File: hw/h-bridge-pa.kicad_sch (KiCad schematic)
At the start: 15 parts, among them Q2301 EPC2037, Q2302 EPC2037, Q2303 IGB110S101XTMA1, Q2304 IGB110S101XTMA1, Q502 IGB110S101XTMA1, Q503 IGB110S101XTMA1, U2301 LMG1210RVRR, U503 LMG1210RVRR

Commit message: Now using H bridge for differential QSE based I/Q tx
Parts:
- T2301: renamed from T502; symbol Device:L_Ferrite_Coupled_Small -> Device:L_Iron_Coupled
- renumbered C2302 to C2301, C2304 to C2302, C2305 to C2304, C2301 to C2305, Q502 to Q2303, Q503 to Q2304, Q2303 to Q2305, Q2304 to Q2306, U503 to U2301, U2301 to U2302
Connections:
- net at Q2303.10 (S), Q2303.11 (S), Q2303.12 (S)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: now also C2305.2, U2301.13 (HS), U2301.14 (HS), U2301.16 (HS), U2301.21 (HS_DAP), U2301.9 (HS)
- net at Q2305.10 (S), Q2305.11 (S), Q2305.12 (S)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: now also C2306.2, U2302.13 (HS), U2302.14 (HS), U2302.16 (HS), U2302.21 (HS_DAP), U2302.9 (HS)
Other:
- moved on the sheet: C2301, C2302, C2303, C2304, C2305, C2306, Q2301, Q2302, Q2303, Q2304, Q2305, Q2306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

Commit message: Trying some sims to make sure tx will work as specified
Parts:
- C2301, C2302, C2303, C2304, C2305, C2306: footprint (none) -> Capacitor_SMD:C_0805_2012Metric
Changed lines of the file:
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@@
 			)
 		)
-		(property "Footprint" ""
+		(property "Footprint" "Capacitor_SMD:C_0805_2012Metric"
 			(at 32.0548 130.81 0)
 			(effects
@@
 				)
 				(hide yes)
+			)
+		)
+		(property "cap-type" ""
+			(at 33.02 127 0)
+			(effects
+				(font
+					(size 1.27 1.27)
+				)
+			)
+		)
+		(property "r-power" ""
+			(at 33.02 127 0)
+			(effects
+				(font
+					(size 1.27 1.27)
+				)
 			)
 		)
@@
 			)
 		)
-		(property "Footprint" ""
+		(property "Footprint" "Capacitor_SMD:C_0805_2012Metric"
 			(at 32.0548 46.99 0)
 			(effects
@@
 				)
 				(hide yes)
+			)
+		)
+		(property "cap-type" ""
+			(at 33.02 43.18 0)
+			(effects
+				(font
+					(size 1.27 1.27)
+				)
+			)
+		)
+		(property "r-power" ""
+			(at 33.02 43.18 0)
+			(effects
+				(font
+					(size 1.27 1.27)
+				)
 			)
 		)
@@
 			)
 		)
-		(property "Footprint" ""
+		(property "Footprint" "Capacitor_SMD:C_0805_2012Metric"
 			(at 39.0652 130.81 0)
 			(effects
@@
 			)
 		)
-		(property "Footprint" ""
+		(property "Footprint" "Capacitor_SMD:C_0805_2012Metric"
 			(at 98.0948 50.8 0)
 			(effects
@@
 			)
 		)
-		(property "Footprint" ""
+		(property "Footprint" "Capacitor_SMD:C_0805_2012Metric"
 			(at 98.0948 134.62 0)
 			(effects
@@
 			)
 		)
-		(property "Footprint" ""
+		(property "Footprint" "Capacitor_SMD:C_0805_2012Metric"
 			(at 39.0652 46.99 0)
 			(effects

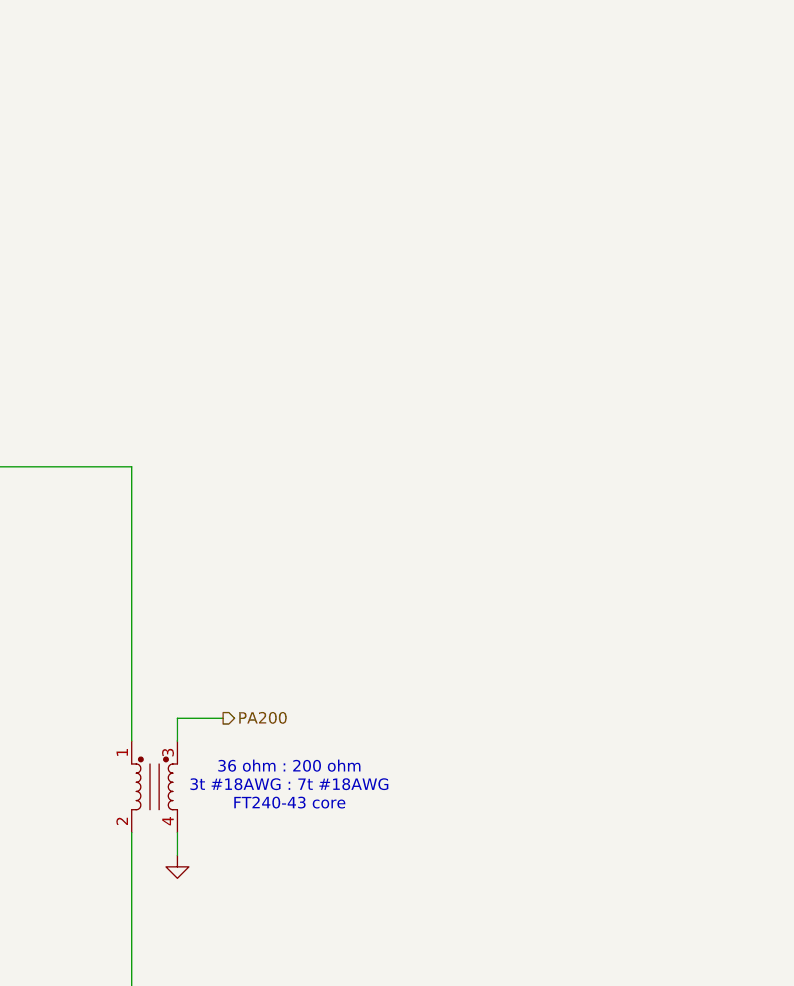
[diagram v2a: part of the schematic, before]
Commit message: Removed PA tanks. LPFs are now 7th order Chebyshev and we are better than -70dBc. Added 0R to power rails for measuring and other testing (did not dare do that for Veer). PCB is now grouped by function to get ready for layout. Still need to verify and set C working voltage levels and choose L and C components for the LPFs. Now using smaller relays at a slight cost premium.
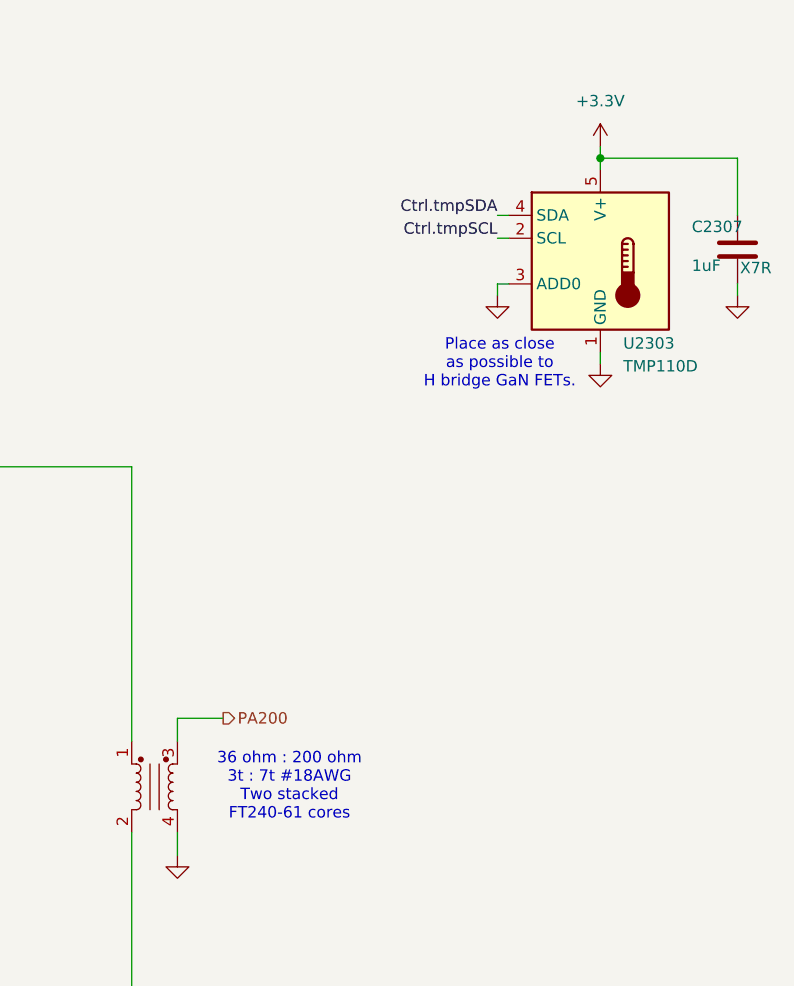
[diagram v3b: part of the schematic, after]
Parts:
- added C2307: 1uF, Capacitor_SMD:C_0805_2012Metric, symbol Device:C
- added U2303: TMP110D, Package_SON:Texas_X2SON-5_0.8x0.8mm_P0.48mm, symbol Sensor_Temperature:TMP110D
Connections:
- net GND: now also C2307.2, U2303.1 (GND), U2303.3 (ADD0)
- new net +3.3V: C2307.1, U2303.5 (V+)
- new net Ctrl.tmpSCL: U2303.2 (SCL)
- new net Ctrl.tmpSDA: U2303.4 (SDA)
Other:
- note added: "36 ohm : 200 ohm 3t : 7t #18AWG Two stacked FT240-61 cores"
- note added: "Place as close as possible to H bridge GaN FETs."
- note removed: "36 ohm : 200 ohm 3t #18AWG : 7t #18AWG FT240-43 core"

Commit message: Starting layout a bit
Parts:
- T2301: footprint Inductor_THT:L_CommonMode_Toroid_Vertical_L38.1mm_W20.3mm_Px15.24mm_Py22.86mm_Bourns_8100 -> Library:2xFT240-stacked
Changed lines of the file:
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@@
 		(dnp no)
 		(property "Reference" "T2301"
-			(at 167.894 102.87 90)
+			(at 173.736 98.552 0)
 			(effects
 				(font
@@
 				)
 				(justify right)
-				(hide yes)
 			)
 		)
@@
 			)
 		)
-		(property "Footprint" "Inductor_THT:L_CommonMode_Toroid_Vertical_L38.1mm_W20.3mm_Px15.24mm_Py22.86mm_Bourns_8100"
+		(property "Footprint" "Library:2xFT240-stacked"
 			(at 173.99 102.87 0)
 			(effects

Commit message: Continuing to route. Net classes can be rather important.
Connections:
- net GND: now also Q2304.10 (S), Q2304.11 (S), Q2304.12 (S), Q2304.3 (S), Q2304.4 (S), Q2304.6 (S), Q2304.7 (S), Q2304.8 (S), Q2304.9 (S), Q2306.10 (S), Q2306.11 (S), Q2306.12 (S), Q2306.3 (S), Q2306.4 (S), Q2306.6 (S), Q2306.7 (S), Q2306.8 (S), Q2306.9 (S)

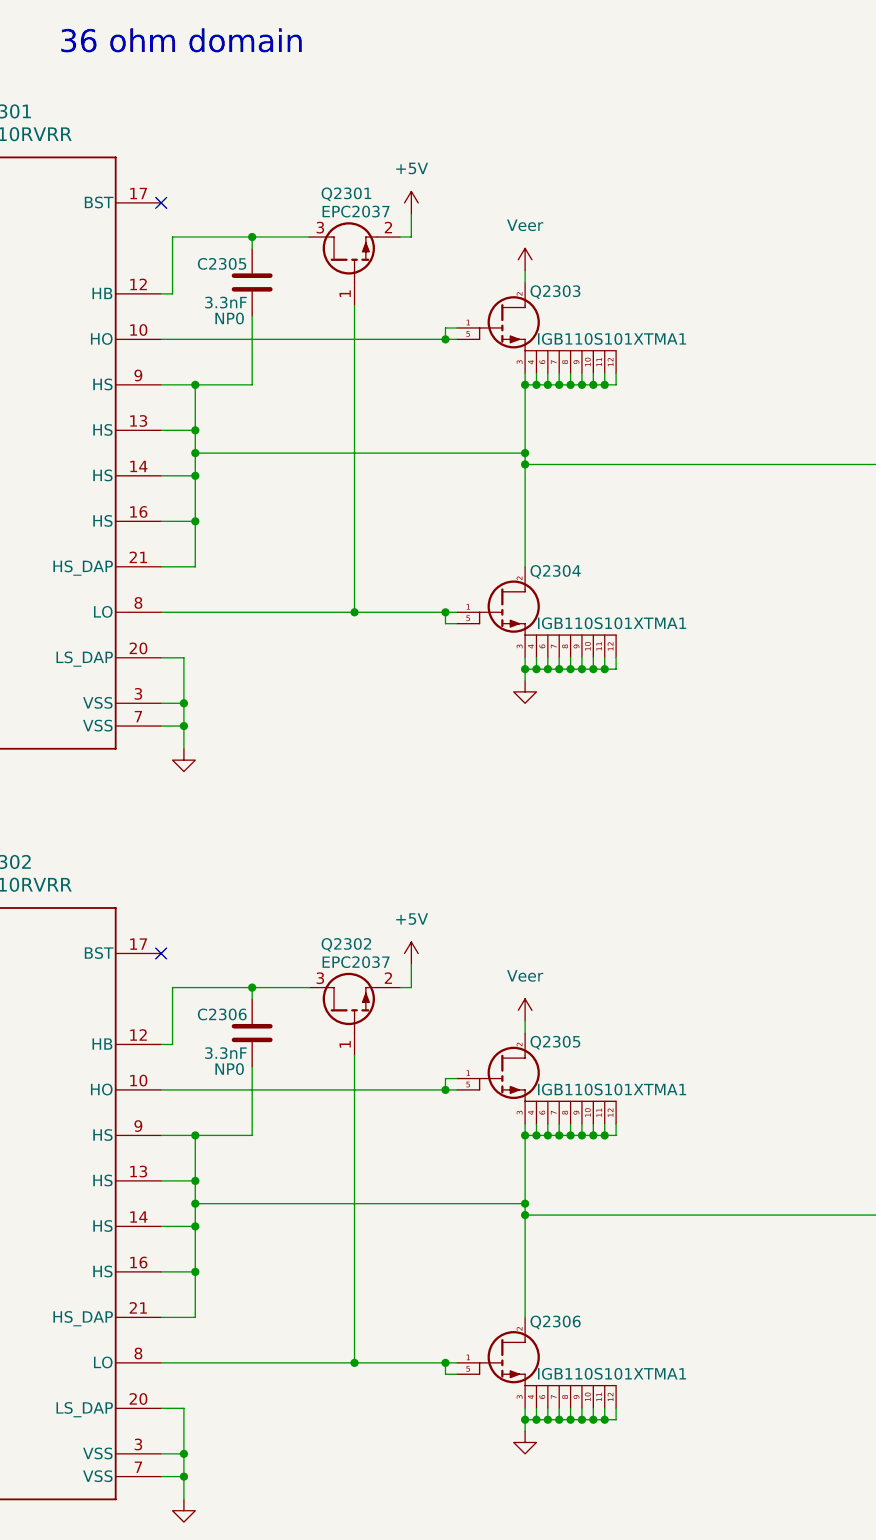
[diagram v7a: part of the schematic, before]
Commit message: I laid down three QSDs but have not done any canyon for 800 ohm yet. Starting to look at Veer buck/boost to round out my understanding.
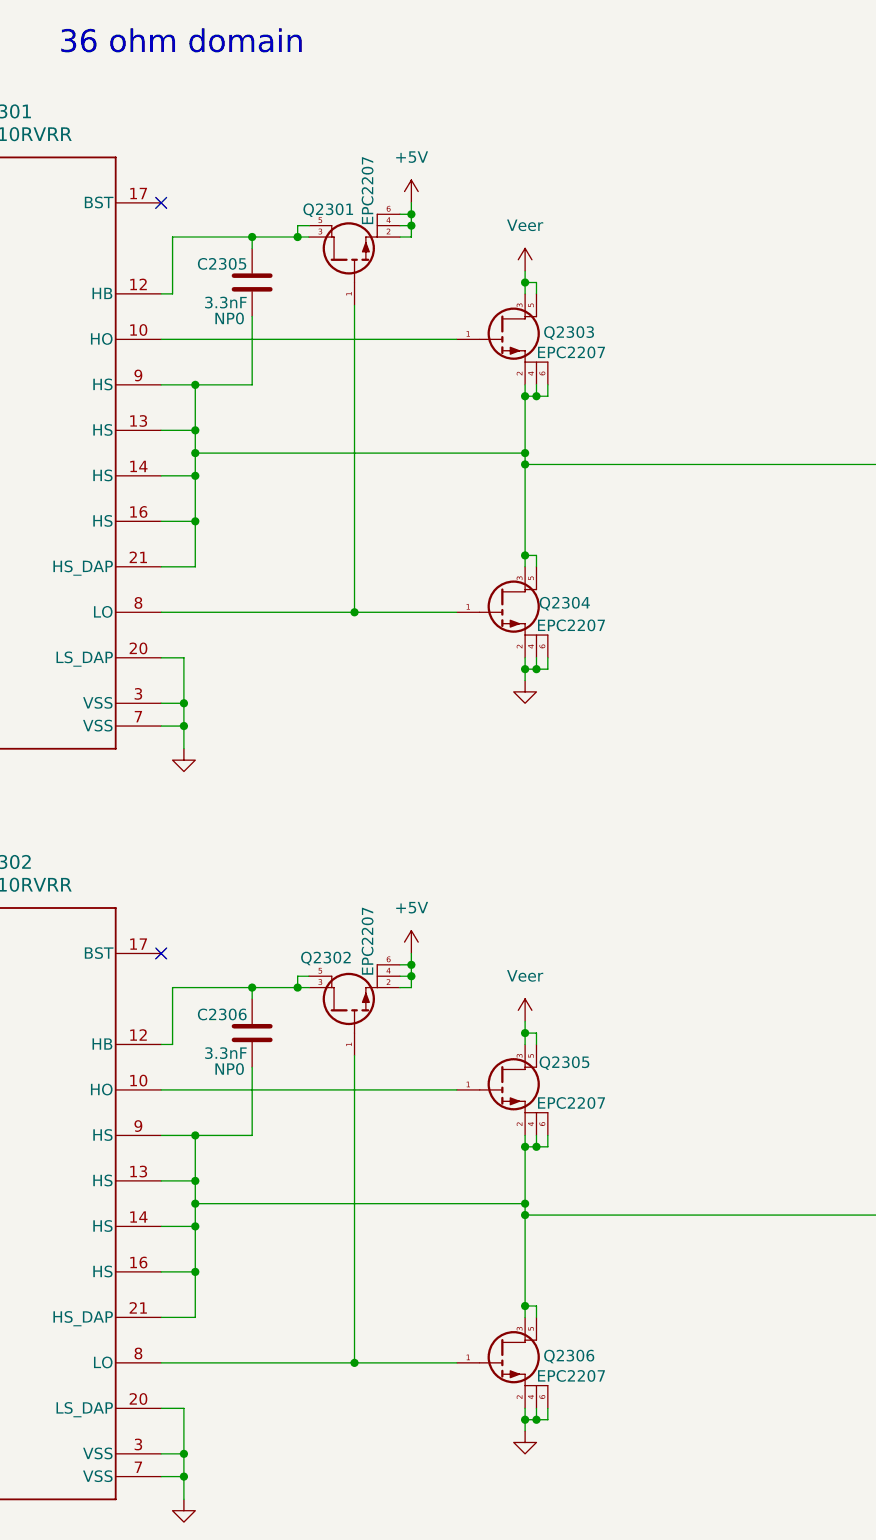
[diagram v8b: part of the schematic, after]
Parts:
- Q2301, Q2302: value EPC2037 -> EPC2207; footprint Package_BGA:EPC_BGA-4_0.9x0.9mm_Layout2x2_P0.45mm -> Library:EPC2207-GaN-FET; symbol Transistor_FET:EPC2037 -> Library:EPC2207-GaN-FET; Height (none) -> 1; Manufacturer_Name (none) -> Infineon; Manufacturer_Part_Number (none) -> IGB110S101XTMA1
- Q2303, Q2304, Q2305, Q2306: value IGB110S101XTMA1 -> EPC2207; footprint IGB110S101XTMA1 -> Library:EPC2207-GaN-FET; symbol Library:IGB110S101XTMA1 -> Library:EPC2207-GaN-FET
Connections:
- net +5V: now also Q2301.6 (S), Q2302.6 (S)
- net GND: now also Q2304.2 (S), Q2306.2 (S); no longer Q2304.10 (S), Q2304.11 (S), Q2304.12 (S), Q2304.3 (S), Q2304.7 (S), Q2304.8 (S), Q2304.9 (S), Q2306.10 (S), Q2306.11 (S), Q2306.12 (S), Q2306.3 (S), Q2306.7 (S), Q2306.8 (S), Q2306.9 (S)
- net Veer: now also Q2303.3 (D), Q2303.5 (D), Q2305.3 (D), Q2305.5 (D); no longer Q2303.2 (D), Q2305.2 (D)
- net at C2305.2, Q2303.4 (S), Q2303.6 (S)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: now also Q2303.2 (S), Q2304.3 (D), Q2304.5 (D); no longer Q2303.10 (S), Q2303.11 (S), Q2303.12 (S), Q2303.3 (S), Q2303.7 (S), Q2303.8 (S), Q2303.9 (S), Q2304.2 (D)
- net at C2306.2, Q2305.4 (S), Q2305.6 (S)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: now also Q2305.2 (S), Q2306.3 (D), Q2306.5 (D); no longer Q2305.10 (S), Q2305.11 (S), Q2305.12 (S), Q2305.3 (S), Q2305.7 (S), Q2305.8 (S), Q2305.9 (S), Q2306.2 (D)
- net at Q2305.1 (G), U2302.10 (HO): no longer Q2305.5 (G)
- net at C2306.1, Q2302.3 (D), U2302.12 (HB): now also Q2302.5 (D)
- net at Q2302.1 (G), Q2306.1 (G), U2302.8 (LO): no longer Q2306.5 (G)
- net at Q2303.1 (G), U2301.10 (HO): no longer Q2303.5 (G)
- net at C2305.1, Q2301.3 (D), U2301.12 (HB): now also Q2301.5 (D)
- net at Q2301.1 (G), Q2304.1 (G), U2301.8 (LO): no longer Q2304.5 (G)
